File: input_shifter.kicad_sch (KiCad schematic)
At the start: 4 parts, among them U5 74HC165

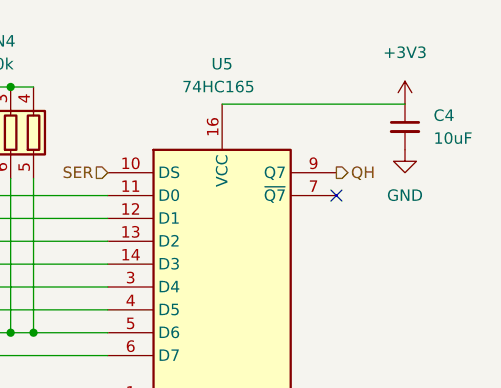
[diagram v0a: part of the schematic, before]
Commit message: Initial board layout, still a lot of work to do
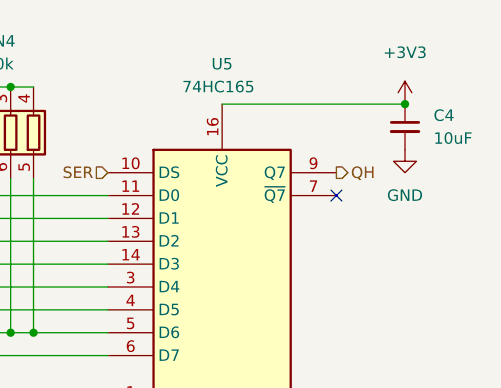
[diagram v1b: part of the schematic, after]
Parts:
- RN3, RN4: footprint CJ4-Autopilot:SW_PUSH_6mm -> Resistor_SMD:R_Array_Convex_4x0603
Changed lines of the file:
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@@
   (junction (at 85.09 71.755) (diameter 0) (color 0 0 0 0)
+  )
+  (junction (at 131.445 48.895) (diameter 0) (color 0 0 0 0)
   )
   (junction (at 74.93 46.99) (diameter 0) (color 0 0 0 0)
@@
     (stroke (width 0) (type default) (color 0 0 0 0))
   )
+  (wire (pts (xy 68.58 46.99) (xy 72.39 46.99))
+    (stroke (width 0) (type default) (color 0 0 0 0))
+  )
+  (wire (pts (xy 80.01 57.15) (xy 80.01 66.675))
+    (stroke (width 0) (type default) (color 0 0 0 0))
+  )
+  (wire (pts (xy 77.47 46.99) (xy 80.01 46.99))
+    (stroke (width 0) (type default) (color 0 0 0 0))
+  )
+  (wire (pts (xy 72.39 46.99) (xy 74.93 46.99))
+    (stroke (width 0) (type default) (color 0 0 0 0))
+  )
+  (wire (pts (xy 70.485 59.055) (xy 72.39 59.055))
+    (stroke (width 0) (type default) (color 0 0 0 0))
+  )
+  (wire (pts (xy 68.58 46.99) (xy 68.58 45.72))
+    (stroke (width 0) (type default) (color 0 0 0 0))
+  )
+  (wire (pts (xy 74.93 61.595) (xy 98.425 61.595))
+    (stroke (width 0) (type default) (color 0 0 0 0))
+  )
+  (wire (pts (xy 87.63 46.99) (xy 90.17 46.99))
+    (stroke (width 0) (type default) (color 0 0 0 0))
+  )
+  (wire (pts (xy 98.425 97.155) (xy 111.125 97.155))
+    (stroke (width 0) (type default) (color 0 0 0 0))
+  )
+  (wire (pts (xy 87.63 74.295) (xy 90.17 74.295))
+    (stroke (width 0) (type default) (color 0 0 0 0))
+  )
+  (wire (pts (xy 82.55 69.215) (xy 98.425 69.215))
+    (stroke (width 0) (type default) (color 0 0 0 0))
+  )
+  (wire (pts (xy 77.47 57.15) (xy 77.47 64.135))
+    (stroke (width 0) (type default) (color 0 0 0 0))
+  )
+  (wire (pts (xy 70.485 74.295) (xy 87.63 74.295))
+    (stroke (width 0) (type default) (color 0 0 0 0))
+  )
+  (wire (pts (xy 77.47 64.135) (xy 98.425 64.135))
+    (stroke (width 0) (type default) (color 0 0 0 0))
+  )
+  (wire (pts (xy 70.485 66.675) (xy 80.01 66.675))
+    (stroke (width 0) (type default) (color 0 0 0 0))
+  )
+  (wire (pts (xy 80.01 66.675) (xy 98.425 66.675))
+    (stroke (width 0) (type default) (color 0 0 0 0))
+  )
+  (wire (pts (xy 70.485 71.755) (xy 85.09 71.755))
+    (stroke (width 0) (type default) (color 0 0 0 0))
+  )
+  (wire (pts (xy 74.93 57.15) (xy 74.93 61.595))
+    (stroke (width 0) (type default) (color 0 0 0 0))
+  )
   (wire (pts (xy 111.125 48.895) (xy 131.445 48.895))
-    (stroke (width 0) (type default) (color 0 0 0 0))
-  )
-  (wire (pts (xy 68.58 46.99) (xy 72.39 46.99))
-    (stroke (width 0) (type default) (color 0 0 0 0))
-  )
-  (wire (pts (xy 80.01 57.15) (xy 80.01 66.675))
-    (stroke (width 0) (type default) (color 0 0 0 0))
-  )
-  (wire (pts (xy 77.47 46.99) (xy 80.01 46.99))
-    (stroke (width 0) (type default) (color 0 0 0 0))
-  )
-  (wire (pts (xy 72.39 46.99) (xy 74.93 46.99))
-    (stroke (width 0) (type default) (color 0 0 0 0))
-  )
-  (wire (pts (xy 70.485 59.055) (xy 72.39 59.055))
-    (stroke (width 0) (type default) (color 0 0 0 0))
-  )
-  (wire (pts (xy 68.58 46.99) (xy 68.58 45.72))
-    (stroke (width 0) (type default) (color 0 0 0 0))
-  )
-  (wire (pts (xy 74.93 61.595) (xy 98.425 61.595))
-    (stroke (width 0) (type default) (color 0 0 0 0))
-  )
-  (wire (pts (xy 87.63 46.99) (xy 90.17 46.99))
-    (stroke (width 0) (type default) (color 0 0 0 0))
-  )
-  (wire (pts (xy 98.425 97.155) (xy 111.125 97.155))
-    (stroke (width 0) (type default) (color 0 0 0 0))
-  )
-  (wire (pts (xy 87.63 74.295) (xy 90.17 74.295))
-    (stroke (width 0) (type default) (color 0 0 0 0))
-  )
-  (wire (pts (xy 82.55 69.215) (xy 98.425 69.215))
-    (stroke (width 0) (type default) (color 0 0 0 0))
-  )
-  (wire (pts (xy 77.47 57.15) (xy 77.47 64.135))
-    (stroke (width 0) (type default) (color 0 0 0 0))
-  )
-  (wire (pts (xy 70.485 74.295) (xy 87.63 74.295))
-    (stroke (width 0) (type default) (color 0 0 0 0))
-  )
-  (wire (pts (xy 77.47 64.135) (xy 98.425 64.135))
-    (stroke (width 0) (type default) (color 0 0 0 0))
-  )
-  (wire (pts (xy 70.485 66.675) (xy 80.01 66.675))
-    (stroke (width 0) (type default) (color 0 0 0 0))
-  )
-  (wire (pts (xy 80.01 66.675) (xy 98.425 66.675))
-    (stroke (width 0) (type default) (color 0 0 0 0))
-  )
-  (wire (pts (xy 70.485 71.755) (xy 85.09 71.755))
-    (stroke (width 0) (type default) (color 0 0 0 0))
-  )
-  (wire (pts (xy 74.93 57.15) (xy 74.93 61.595))
     (stroke (width 0) (type default) (color 0 0 0 0))
   )
@@
     (property "Reference" "RN3" (id 0) (at 76.2 41.91 0))
     (property "Value" "10k" (id 1) (at 76.2 44.45 0))
-    (property "Footprint" "CJ4-Autopilot:SW_PUSH_6mm" (id 2) (at 84.455 52.07 90)
+    (property "Footprint" "Resistor_SMD:R_Array_Convex_4x0603" (id 2) (at 84.455 52.07 90)
       (effects (font (size 1.27 1.27)) hide)
     )
@@
     (property "Reference" "RN4" (id 0) (at 86.36 41.91 0))
     (property "Value" "10k" (id 1) (at 86.36 44.45 0))
-    (property "Footprint" "CJ4-Autopilot:SW_PUSH_6mm" (id 2) (at 94.615 52.07 90)
-      (effects (font (size 1.27 1.27)) hide)
-    )
+    (property "Footprint" "Resistor_SMD:R_Array_Convex_4x0603" (id 2) (at 94.615 52.07 90)
+      (effects (font (size 1.27 1.27)) hide)
+    )

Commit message: Add RP2040 directly to the board
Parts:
- C4: JLC (none) -> 0603; LCSC (none) -> C19702
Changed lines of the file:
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@@
+      (effects (font (size 1.27 1.27)) hide)
+    )
+    (property "JLC" "0603" (id 4) (at 131.445 51.435 0)
+      (effects (font (size 1.27 1.27)) hide)
+    )
+    (property "LCSC" "C19702" (id 5) (at 131.445 51.435 0)
       (effects (font (size 1.27 1.27)) hide)
     )

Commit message: Tons and tons of traces
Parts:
- renumbered C4 to C3, RN3 to RN1, RN4 to RN2, U5 to U4
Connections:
- net D6: no longer RN2.5 (R4.2)
- net D7: now also RN2.5 (R4.2)
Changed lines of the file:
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@@
   (junction (at 72.39 59.055) (diameter 0) (color 0 0 0 0)
   )
-  (junction (at 90.17 74.295) (diameter 0) (color 0 0 0 0)
-  )
   (junction (at 80.01 46.99) (diameter 0) (color 0 0 0 0)
   )
@@
   )
   (junction (at 72.39 46.99) (diameter 0) (color 0 0 0 0)
+  )
+  (junction (at 90.17 76.835) (diameter 0) (color 0 0 0 0)
   )
   (junction (at 87.63 74.295) (diameter 0) (color 0 0 0 0)
@@
     (stroke (width 0) (type default) (color 0 0 0 0))
   )
+  (wire (pts (xy 90.17 76.835) (xy 98.425 76.835))
+    (stroke (width 0) (type default) (color 0 0 0 0))
+  )
   (wire (pts (xy 70.485 59.055) (xy 72.39 59.055))
     (stroke (width 0) (type default) (color 0 0 0 0))
@@
     (stroke (width 0) (type default) (color 0 0 0 0))
   )
-  (wire (pts (xy 87.63 74.295) (xy 90.17 74.295))
-    (stroke (width 0) (type default) (color 0 0 0 0))
-  )
   (wire (pts (xy 82.55 69.215) (xy 98.425 69.215))
     (stroke (width 0) (type default) (color 0 0 0 0))
@@
     (stroke (width 0) (type default) (color 0 0 0 0))
   )
-  (wire (pts (xy 90.17 57.15) (xy 90.17 74.295))
-    (stroke (width 0) (type default) (color 0 0 0 0))
-  )
-  (wire (pts (xy 70.485 76.835) (xy 98.425 76.835))
+  (wire (pts (xy 70.485 76.835) (xy 90.17 76.835))
+    (stroke (width 0) (type default) (color 0 0 0 0))
+  )
+  (wire (pts (xy 90.17 57.15) (xy 90.17 76.835))
     (stroke (width 0) (type default) (color 0 0 0 0))
   )
@@
     (stroke (width 0) (type default) (color 0 0 0 0))
   )
-  (wire (pts (xy 90.17 74.295) (xy 98.425 74.295))
+  (wire (pts (xy 87.63 74.295) (xy 98.425 74.295))
     (stroke (width 0) (type default) (color 0 0 0 0))
   )
@@
   (symbol (lib_id "Device:R_Pack04") (at 77.47 52.07 0) (mirror x)
     (in_bom yes) (on_board yes)
-    (property "Reference" "RN3" (id 0) (at 76.2 41.91 0))
+    (property "Reference" "RN1" (id 0) (at 76.2 41.91 0))
     (property "Value" "10k" (id 1) (at 76.2 44.45 0))
     (property "Footprint" "Resistor_SMD:R_Array_Convex_4x0603" (id 2) (at 84.455 52.07 90)
@@
   (symbol (lib_id "Device:C_Small") (at 131.445 51.435 0)
     (in_bom yes) (on_board yes) (fields_autoplaced)
-    (property "Reference" "C4" (id 0) (at 134.62 50.1712 0)
+    (property "Reference" "C3" (id 0) (at 134.62 50.1712 0)
       (effects (font (size 1.27 1.27)) (justify left))
     )
@@
   (symbol (lib_id "Device:R_Pack04") (at 87.63 52.07 0) (mirror x)
     (in_bom yes) (on_board yes)
-    (property "Reference" "RN4" (id 0) (at 86.36 41.91 0))
+    (property "Reference" "RN2" (id 0) (at 86.36 41.91 0))
     (property "Value" "10k" (id 1) (at 86.36 44.45 0))
     (property "Footprint" "Resistor_SMD:R_Array_Convex_4x0603" (id 2) (at 94.615 52.07 90)
@@
   (symbol (lib_id "74xx:74HC165") (at 111.125 71.755 0)
     (in_bom yes) (on_board yes)
-    (property "Reference" "U5" (id 0) (at 111.125 44.45 0))
+    (property "Reference" "U4" (id 0) (at 111.125 44.45 0))
     (property "Value" "74HC165" (id 1) (at 106.68 46.99 0)
       (effects (font (size 1.27 1.27)) (justify left))

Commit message: Fully routed!
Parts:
- renumbered C3 to C4, RN1 to RN3, RN2 to RN4, U4 to U5
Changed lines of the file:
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@@
   (symbol (lib_id "Device:R_Pack04") (at 77.47 52.07 0) (mirror x)
     (in_bom yes) (on_board yes)
-    (property "Reference" "RN1" (id 0) (at 76.2 41.91 0))
+    (property "Reference" "RN3" (id 0) (at 76.2 41.91 0))
     (property "Value" "10k" (id 1) (at 76.2 44.45 0))
     (property "Footprint" "Resistor_SMD:R_Array_Convex_4x0603" (id 2) (at 84.455 52.07 90)
@@
   (symbol (lib_id "Device:C_Small") (at 131.445 51.435 0)
     (in_bom yes) (on_board yes) (fields_autoplaced)
-    (property "Reference" "C3" (id 0) (at 134.62 50.1712 0)
+    (property "Reference" "C4" (id 0) (at 134.62 50.1712 0)
       (effects (font (size 1.27 1.27)) (justify left))
     )
@@
   (symbol (lib_id "Device:R_Pack04") (at 87.63 52.07 0) (mirror x)
     (in_bom yes) (on_board yes)
-    (property "Reference" "RN2" (id 0) (at 86.36 41.91 0))
+    (property "Reference" "RN4" (id 0) (at 86.36 41.91 0))
     (property "Value" "10k" (id 1) (at 86.36 44.45 0))
     (property "Footprint" "Resistor_SMD:R_Array_Convex_4x0603" (id 2) (at 94.615 52.07 90)
@@
   (symbol (lib_id "74xx:74HC165") (at 111.125 71.755 0)
     (in_bom yes) (on_board yes)
-    (property "Reference" "U4" (id 0) (at 111.125 44.45 0))
+    (property "Reference" "U5" (id 0) (at 111.125 44.45 0))
     (property "Value" "74HC165" (id 1) (at 106.68 46.99 0)
       (effects (font (size 1.27 1.27)) (justify left))
